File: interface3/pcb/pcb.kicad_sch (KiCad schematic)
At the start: 27 parts, among them J1 Conn_Coaxial, T1 Murata 78602/8JC, U1 DS34LV86T, U2 DS34LV87T, U3 Pico_W

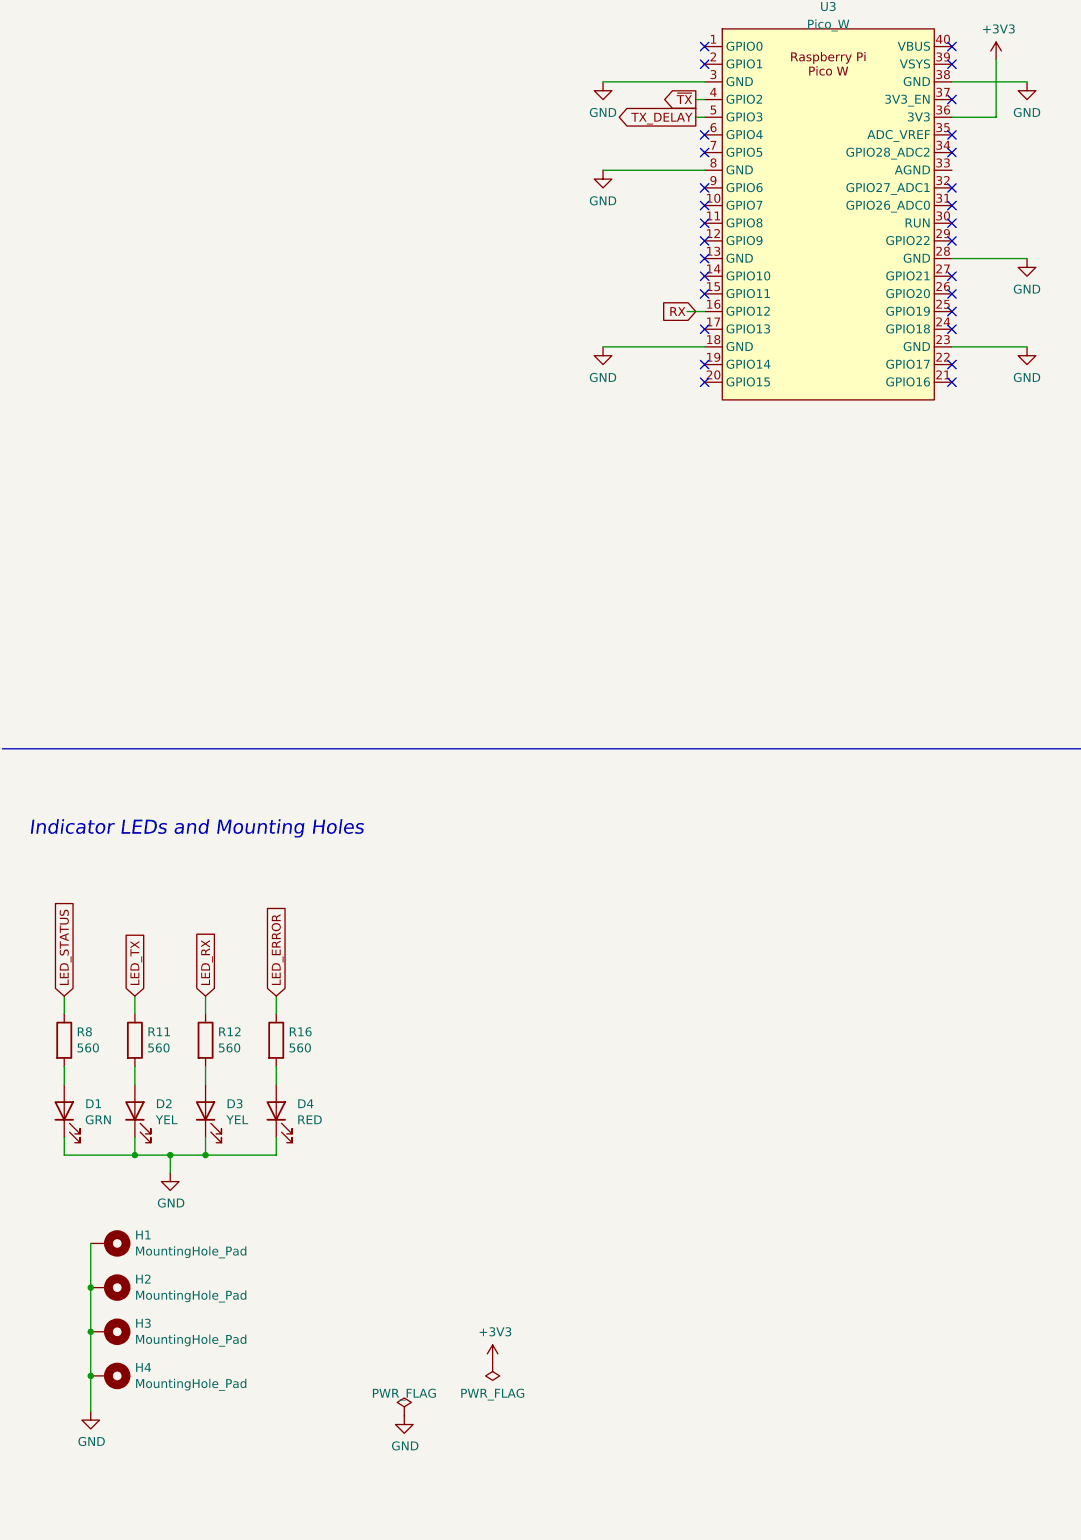
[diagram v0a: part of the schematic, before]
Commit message: improve interface3 schematic, unify pin names
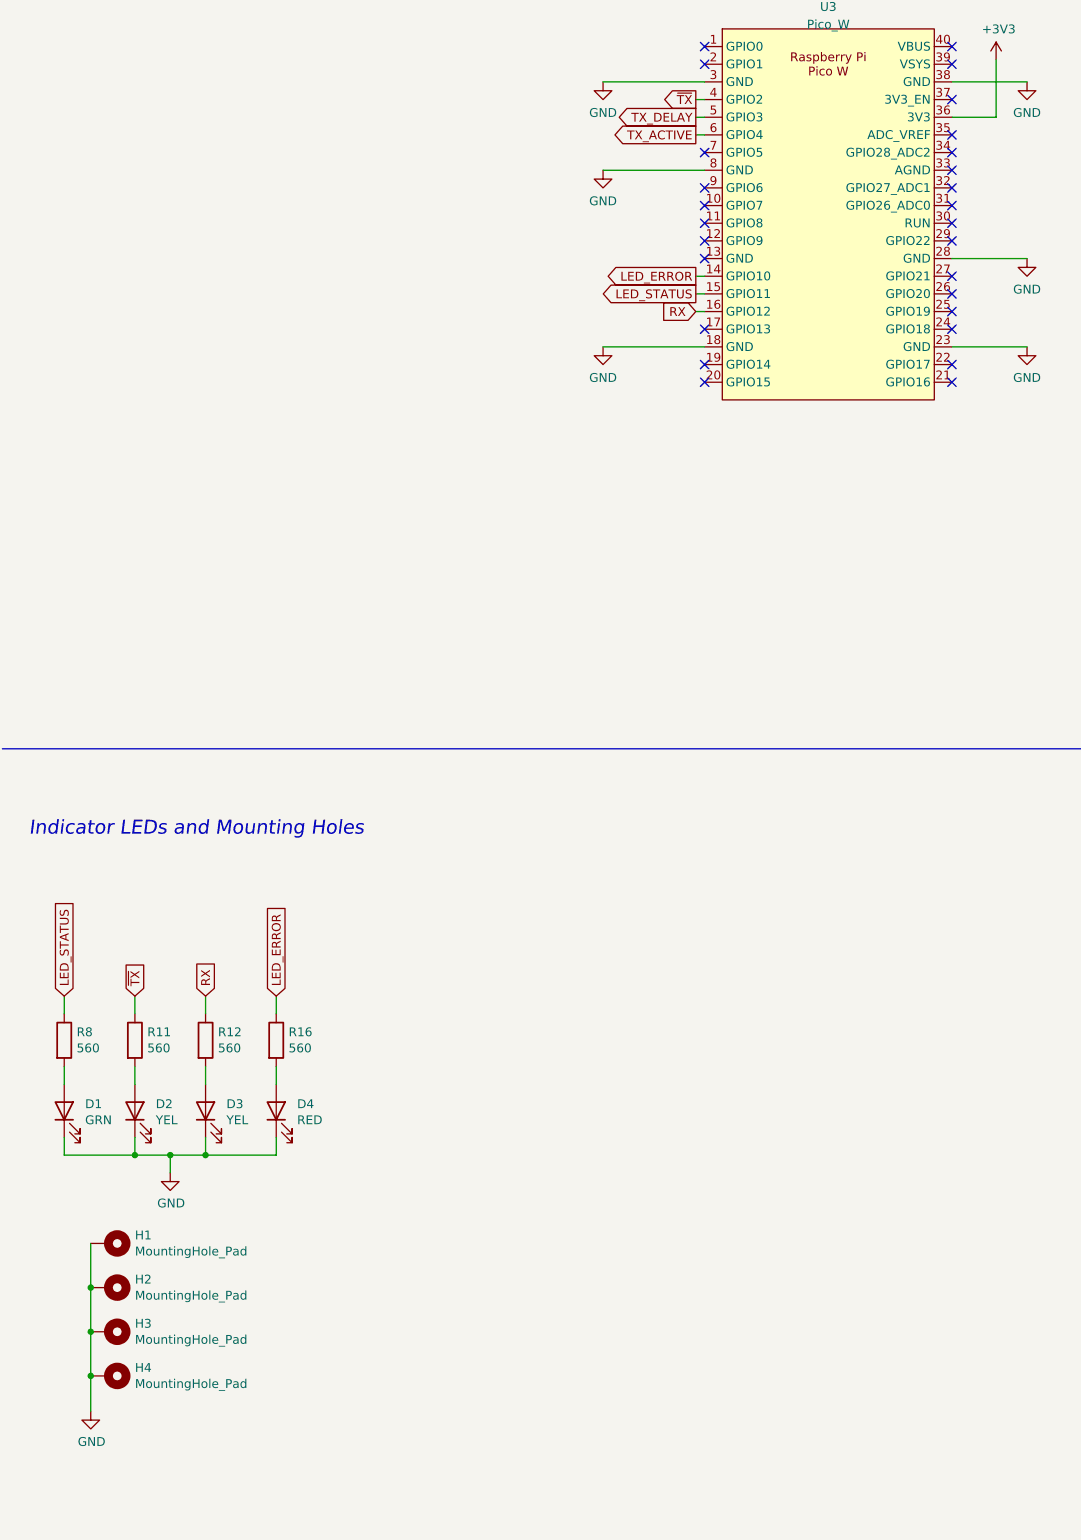
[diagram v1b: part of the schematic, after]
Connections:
- net LED_RX is gone; now on net RX: R12.1
- net LED_TX is gone; now on net ~{TX}: R11.1
- net LED_ERROR: now also U3.14 (GPIO10)
- net LED_STATUS: now also U3.15 (GPIO11)
- net TX_ACTIVE: now also U3.6 (GPIO4)
- no-connect marks 36 -> 34
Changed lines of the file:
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@@
   (no_connect (at 123.19 71.755))
   (no_connect (at 123.19 97.155))
-  (no_connect (at 123.19 81.915))
   (no_connect (at 123.19 84.455))
   (no_connect (at 346.71 207.01))
+  (no_connect (at 158.75 86.995))
   (no_connect (at 123.19 99.695))
   (no_connect (at 123.19 69.215))
@@
   (no_connect (at 158.75 114.935))
   (no_connect (at 346.71 212.09))
-  (no_connect (at 123.19 104.775))
   (no_connect (at 158.75 97.155))
   (no_connect (at 158.75 109.855))
@@
   (no_connect (at 314.96 212.09))
   (no_connect (at 158.75 71.755))
-  (no_connect (at 123.19 102.235))
   (no_connect (at 123.19 94.615))
   (no_connect (at 158.75 104.775))
@@
     (stroke (width 0) (type default))
   )
+  (wire (pts (xy 121.92 81.915) (xy 123.19 81.915))
+    (stroke (width 0) (type default))
+  )
   (wire (pts (xy 41.275 215.9) (xy 41.275 218.44))
     (stroke (width 0) (type default))
@@
     (stroke (width 0) (type default))
   )
-  (wire (pts (xy 120.65 107.315) (xy 123.19 107.315))
+  (wire (pts (xy 121.92 107.315) (xy 123.19 107.315))
     (stroke (width 0) (type default))
   )
@@
     (stroke (width 0) (type default))
   )
+  (wire (pts (xy 121.92 104.775) (xy 123.19 104.775))
+    (stroke (width 0) (type default))
+  )
   (wire (pts (xy 51.435 226.06) (xy 51.435 228.6))
     (stroke (width 0) (type default))
@@
   )
   (wire (pts (xy 331.47 80.01) (xy 331.47 69.85))
+    (stroke (width 0) (type default))
+  )
+  (wire (pts (xy 121.92 102.235) (xy 123.19 102.235))
     (stroke (width 0) (type default))
   )
@@
     )
   )
+  (global_label "TX_ACTIVE" (shape output) (at 121.92 81.915 180)
+    (effects (font (size 1.27 1.27)) (justify right))
+    (property "Intersheetrefs" "${INTERSHEET_REFS}" (at 121.92 81.915 0)
+      (effects (font (size 1.27 1.27)) hide)
+    )
+  )
   (global_label "TX+" (shape passive) (at 364.49 71.12 180)
     (effects (font (size 1.27 1.27)) (justify right))
@@
     )
   )
+  (global_label "LED_ERROR" (shape output) (at 121.92 102.235 180)
+    (effects (font (size 1.27 1.27)) (justify right))
+    (property "Intersheetrefs" "${INTERSHEET_REFS}" (at 121.92 102.235 0)
+      (effects (font (size 1.27 1.27)) hide)
+    )
+  )
   (global_label "RX-" (shape passive) (at 346.71 46.99 0)
     (effects (font (size 1.27 1.27)) (justify left))
@@
     )
   )
-  (global_label "LED_RX" (shape input) (at 51.435 205.74 90)
+  (global_label "RX" (shape input) (at 51.435 205.74 90)
     (effects (font (size 1.27 1.27)) (justify left))
     (property "Intersheetrefs" "${INTERSHEET_REFS}" (at 51.435 205.74 0)
@@
     )
   )
+  (global_label "LED_STATUS" (shape output) (at 121.92 104.775 180)
+    (effects (font (size 1.27 1.27)) (justify right))
+    (property "Intersheetrefs" "${INTERSHEET_REFS}" (at 121.92 104.775 0)
+      (effects (font (size 1.27 1.27)) hide)
+    )
+  )
   (global_label "TX_DELAY" (shape input) (at 289.56 72.39 180)
     (effects (font (size 1.27 1.27)) (justify right))
@@
     )
   )
-  (global_label "LED_TX" (shape input) (at 41.275 205.74 90)
+  (global_label "~{TX}" (shape input) (at 41.275 205.74 90)
     (effects (font (size 1.27 1.27)) (justify left))
     (property "Intersheetrefs" "${INTERSHEET_REFS}" (at 41.275 205.74 0)
@@
     )
   )
-  (symbol (lib_id "power:GND") (at 80.01 266.065 0) (unit 1)
-    (in_bom yes) (on_board yes) (dnp no)
-    (property "Reference" "#PWR030" (at 80.01 272.415 0)
-      (effects (font (size 1.27 1.27)) hide)
-    )
-    (property "Value" "GND" (at 80.137 270.4592 0)
-      (effects (font (size 1.27 1.27)))
-    )
-    (property "Footprint" "" (at 80.01 266.065 0)
-      (effects (font (size 1.27 1.27)) hide)
-    )
-    (property "Datasheet" "" (at 80.01 266.065 0)
-      (effects (font (size 1.27 1.27)) hide)
-    )
-    (pin "1")
-    (instances
-      (project "pcb"
-        (path "/526cd2dc-8794-4bb6-97c2-9b545ee4fe34"
-          (reference "#PWR030") (unit 1)
-        )
-      )
-    )
-  )
   (symbol (lib_id "power:GND") (at 169.545 74.295 0) (unit 1)
     (in_bom yes) (on_board yes) (dnp no) (fields_autoplaced)
@@
     )
   )
-  (symbol (lib_id "power:+3V3") (at 92.71 258.445 0) (unit 1)
-    (in_bom yes) (on_board yes) (dnp no)
-    (property "Reference" "#PWR031" (at 92.71 262.255 0)
-      (effects (font (size 1.27 1.27)) hide)
-    )
-    (property "Value" "+3V3" (at 93.091 254.0508 0)
-      (effects (font (size 1.27 1.27)))
-    )
-    (property "Footprint" "" (at 92.71 258.445 0)
-      (effects (font (size 1.27 1.27)) hide)
-    )
-    (property "Datasheet" "" (at 92.71 258.445 0)
-      (effects (font (size 1.27 1.27)) hide)
-    )
-    (pin "1")
-    (instances
-      (project "pcb"
-        (path "/526cd2dc-8794-4bb6-97c2-9b545ee4fe34"
-          (reference "#PWR031") (unit 1)
-        )
-      )
-    )
-  )
-  (symbol (lib_id "power:PWR_FLAG") (at 80.01 266.065 0) (unit 1)
-    (in_bom yes) (on_board yes) (dnp no) (fields_autoplaced)
-    (property "Reference" "#FLG01" (at 80.01 264.16 0)
-      (effects (font (size 1.27 1.27)) hide)
-    )
-    (property "Value" "PWR_FLAG" (at 80.01 262.89 0)
-      (effects (font (size 1.27 1.27)))
-    )
-    (property "Footprint" "" (at 80.01 266.065 0)
-      (effects (font (size 1.27 1.27)) hide)
-    )
-    (property "Datasheet" "~" (at 80.01 266.065 0)
-      (effects (font (size 1.27 1.27)) hide)
-    )
-    (pin "1")
-    (instances
-      (project "pcb"
-        (path "/526cd2dc-8794-4bb6-97c2-9b545ee4fe34"
-          (reference "#FLG01") (unit 1)
-        )
-      )
-    )
-  )
   (symbol (lib_id "power:GND") (at 108.585 86.995 0) (unit 1)
     (in_bom yes) (on_board yes) (dnp no) (fields_autoplaced)
@@
         )
       )
-    )
-  )
-  (symbol (lib_id "power:PWR_FLAG") (at 92.71 258.445 180) (unit 1)
-    (in_bom yes) (on_board yes) (dnp no) (fields_autoplaced)
-    (property "Reference" "#FLG02" (at 92.71 260.35 0)
-      (effects (font (size 1.27 1.27)) hide)
-    )
-    (property "Value" "PWR_FLAG" (at 92.71 262.89 0)
-      (effects (font (size 1.27 1.27)))
-    )
-    (property "Footprint" "" (at 92.71 258.445 0)
-      (effects (font (size 1.27 1.27)) hide)
-    )
-    (property "Datasheet" "~" (at 92.71 258.445 0)
-      (effects (font (size 1.27 1.27)) hide)
-    )
-    (pin "1")
-    (instances
-      (project "pcb"
-        (path "/526cd2dc-8794-4bb6-97c2-9b545ee4fe34"
-          (reference "#FLG02") (unit 1)
-        )
-      )

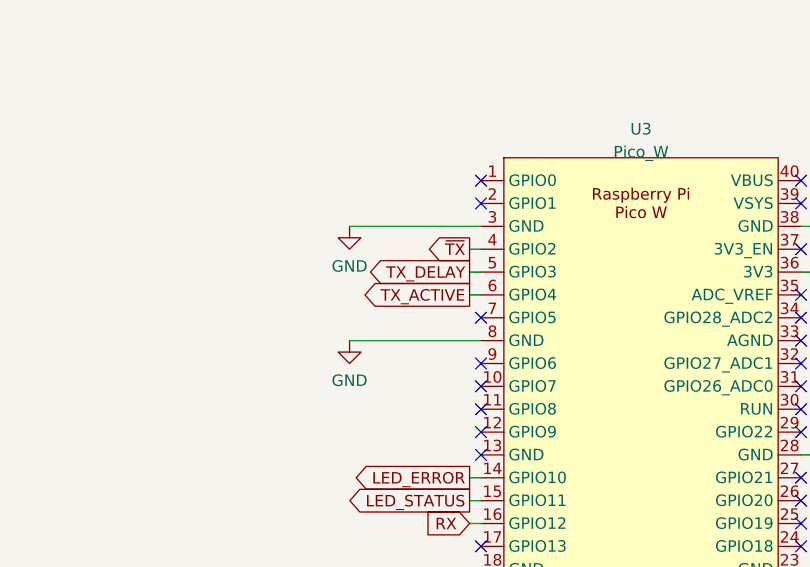
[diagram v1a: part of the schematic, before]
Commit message: generate TX_ACTIVE signal
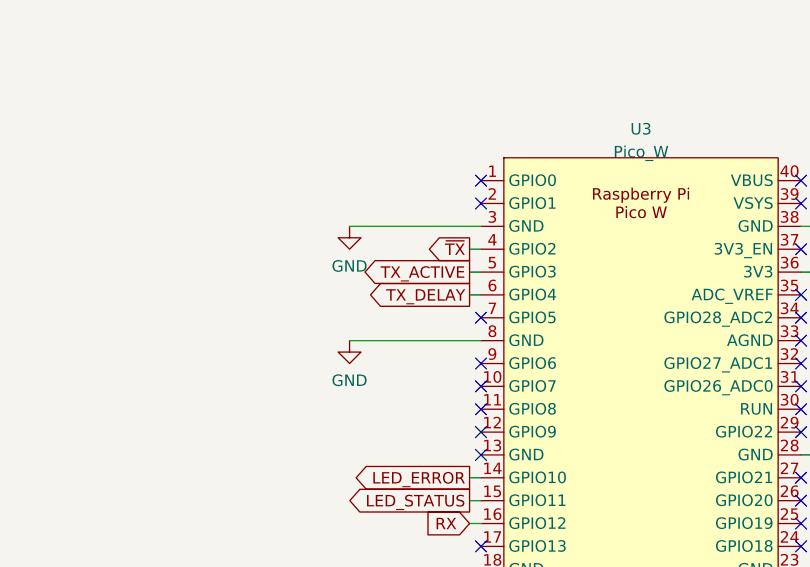
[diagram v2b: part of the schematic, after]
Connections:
- net TX_ACTIVE: now also U3.5 (GPIO3); no longer U3.6 (GPIO4)
- net TX_DELAY: now also U3.6 (GPIO4); no longer U3.5 (GPIO3)
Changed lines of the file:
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@@
     )
   )
-  (global_label "TX_DELAY" (shape output) (at 121.92 79.375 180)
+  (global_label "TX_DELAY" (shape output) (at 121.92 81.915 180)
     (effects (font (size 1.27 1.27)) (justify right))
-    (property "Intersheetrefs" "${INTERSHEET_REFS}" (at 121.92 79.375 0)
+    (property "Intersheetrefs" "${INTERSHEET_REFS}" (at 121.92 81.915 0)
       (effects (font (size 1.27 1.27)) hide)
     )
@@
     )
   )
-  (global_label "TX_ACTIVE" (shape output) (at 121.92 81.915 180)
+  (global_label "TX_ACTIVE" (shape output) (at 121.92 79.375 180)
     (effects (font (size 1.27 1.27)) (justify right))
-    (property "Intersheetrefs" "${INTERSHEET_REFS}" (at 121.92 81.915 0)
+    (property "Intersheetrefs" "${INTERSHEET_REFS}" (at 121.92 79.375 0)
       (effects (font (size 1.27 1.27)) hide)
     )
